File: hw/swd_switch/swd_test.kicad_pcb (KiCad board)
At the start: 2 copper layers, 30 x 17 mm, 11 parts, among them J1 SWD_IN, J2 Conn_01x04, J3 SWD_PWR, J4 SWD_OUT, U1 SN74LVC2G66, U2 SN74LVC2G66, U3 SN74LVC2G66

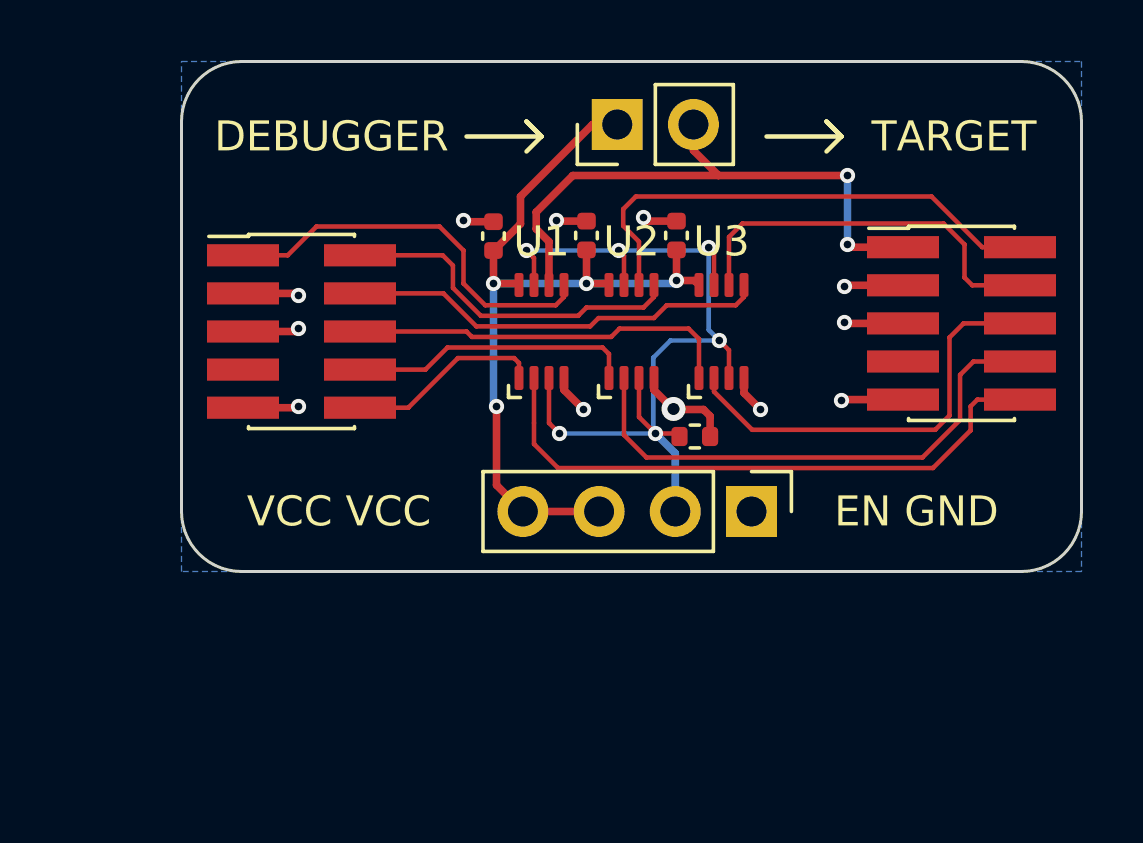
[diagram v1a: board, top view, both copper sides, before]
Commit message: Updated debugotron v2.0 and ordered
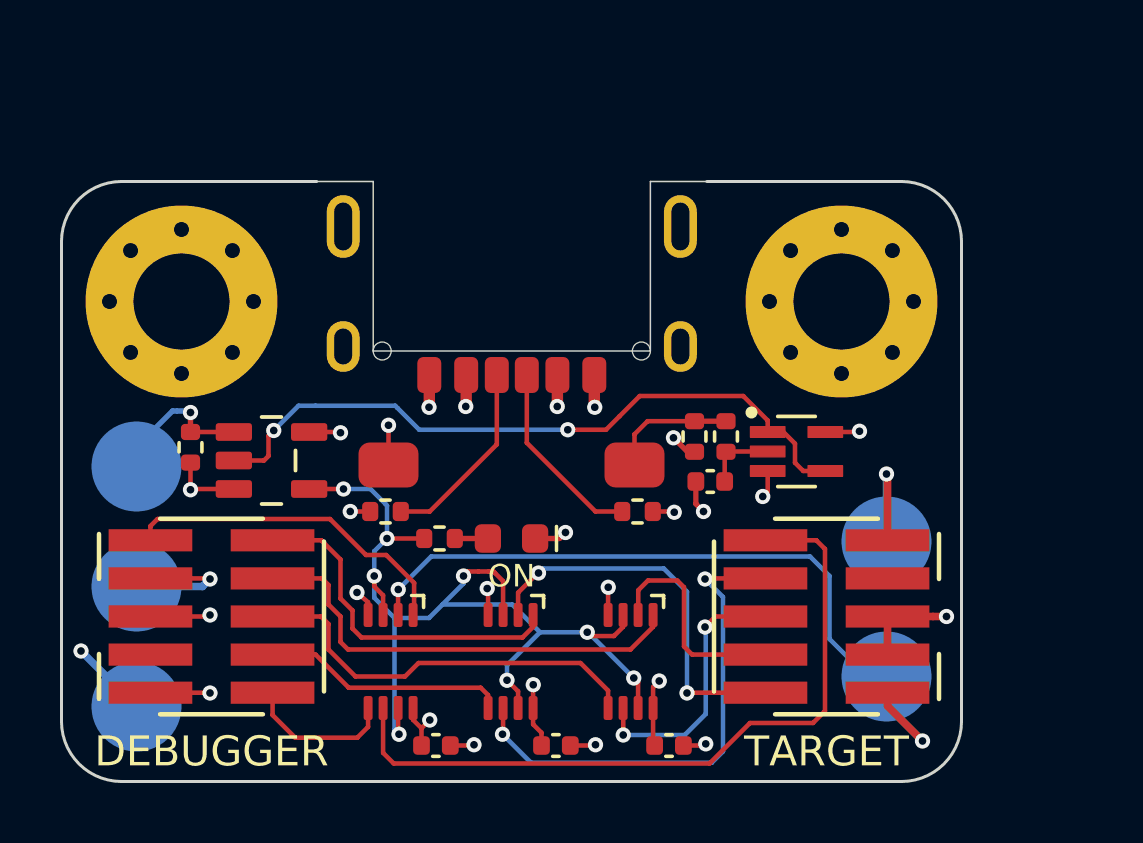
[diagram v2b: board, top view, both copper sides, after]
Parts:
- removed J1: SWD_IN, Connector_PinHeader_1.27mm:PinHeader_2x05_P1.27mm_Vertical_SMD
- removed J4: SWD_OUT, Connector_PinHeader_1.27mm:PinHeader_2x05_P1.27mm_Vertical_SMD
- added C4: 0.1uF, Capacitor_SMD:C_0402_1005Metric, F.Cu at (107.5, 73.8)
- added D1: LED, LED_SMD:LED_0603_1608Metric, F.Cu at (106.0, 66.9)
- added J5: SWD_OUT, snapeda:SAMTEC_FTSH-105-01-F-DV-P-TR_alt, F.Cu at (116.5, 69.5)
- added R1: 5.1k, Resistor_SMD:R_0402_1005Metric, F.Cu at (112.1, 63.5)
- added R3: 5.1k, Resistor_SMD:R_0402_1005Metric, F.Cu at (95.3, 63.9)
- added R4: 5.1k, Resistor_SMD:R_0402_1005Metric, F.Cu at (101.8, 66.0)
- added R5: 5.1k, Resistor_SMD:R_0402_1005Metric, F.Cu at (110.2, 66.0)
- added R6: 5.1k, Resistor_SMD:R_0402_1005Metric, F.Cu at (103.6, 66.9)
- added REF**: MountingHole_3.2mm_M3_Pad_Via, MountingHole:MountingHole_3.2mm_M3_Pad_Via, F.Cu at (117.0, 59.0)
- added REF**: MountingHole_3.2mm_M3_Pad_Via, MountingHole:MountingHole_3.2mm_M3_Pad_Via, F.Cu at (95.0, 59.0)
- added SW1: SW_Push, alvarop:PTS636_G, F.Cu at (106.0, 64.5)
- added TP1: TestPoint, TestPoint:TestPoint_Pad_D3.0mm, B.Cu at (93.5, 72.5)
- added TP2: TestPoint, TestPoint:TestPoint_Pad_D3.0mm, B.Cu at (93.5, 68.5)
- added TP3: TestPoint, TestPoint:TestPoint_Pad_D3.0mm, B.Cu at (93.5, 64.5)
- added TP4: TestPoint, TestPoint:TestPoint_Pad_D3.0mm, B.Cu at (118.5, 67.0)
- added TP5: TestPoint, TestPoint:TestPoint_Pad_D3.0mm, B.Cu at (118.5, 71.5)
- added U4: SN74LVC2G66, alvarop:SN74LVC2G66-VSSOP, F.Cu at (102.0, 71.0)
- added U5: SN74LVC2G66, alvarop:SN74LVC2G66-VSSOP, F.Cu at (106.0, 71.0)
- J2: value Conn_01x04 -> USB_C_Receptacle_USB2.0; footprint Connector_PinHeader_2.54mm:PinHeader_1x04_P2.54mm_Vertical -> alvarop:USB4515-GF-A
- J3: value SWD_PWR -> SWD_IN; footprint Connector_PinHeader_2.54mm:PinHeader_1x02_P2.54mm_Vertical -> snapeda:SAMTEC_FTSH-105-01-F-DV-P-TR_alt
- R2: value 10k -> 5.1k
- U1: value SN74LVC2G66 -> SN74LVC1G80DCKR; footprint alvarop:SN74LVC2G66-VSSOP -> snapeda:SOT65P210X110-5N
- U2: value SN74LVC2G66 -> SN74LVC1G32DBVR; footprint alvarop:SN74LVC2G66-VSSOP -> snapeda:SOT95P280X145-5N
- moved J3 21.3 mm to (96.0, 69.5), turned to -90 degrees
- moved C2 17.7 mm to (103.5, 73.8), turned to 0 degrees
- moved C3 17.0 mm to (111.2, 73.8), turned to 0 degrees
- moved U2 12.7 mm to (98.0, 64.3)
- moved U3 11.4 mm to (110.0, 71.0), turned to 180 degrees
- moved C1 10.9 mm to (112.6, 65.0), turned to 0 degrees
- moved J2 9.70 mm to (106.0, 60.5), turned to 180 degrees
- moved U1 9.39 mm to (115.5, 64.0)
- moved R2 1.04 mm to (113.2, 63.5), turned to -90 degrees
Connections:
- C1 pad 2: GND -> Net-(C1-Pad2)
- J3 pad 1: VCC -> /VREF
- J3 pad 2: /VREF_OUT -> /SWDIO_TMS
- R2 pad 1: /SWD_EN -> Net-(R1-Pad1)
- R2 pad 2: GND -> Net-(C1-Pad2)
- U1 pad 1: /RESET -> /SWD_EN_BTN
- U1 pad 2: /RESET_OUT -> Net-(C1-Pad2)
- U1 pad 3: /SWD_EN -> GND
- U1 pad 4: GND -> /SWD_EN_BTN
- U1 pad 5: /VREF -> VCC
- U2 pad 1: /TDI -> /SWD_EN_EXT
- U2 pad 2: /TDI_OUT -> /SWD_EN_BTN
- U2 pad 3: /SWD_EN -> GND
- U2 pad 4: GND -> /SWD_EN
- U2 pad 5: /SWDIO_TMS -> VCC
- U3 pad 1: /SWO_TDO -> /SWDCLK_TCK
- U3 pad 2: /SWO_TDO_OUT -> /SWDCLK_TCK_OUT
- U3 pad 5: /SWDCLK_TCK -> /SWO_TDO
- U3 pad 6: /SWDCLK_TCK_OUT -> /SWO_TDO_OUT
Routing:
- net /SWD_EN_BTN: track 0.00 -> 23.3 mm, vias 0 -> 2
- net VCC: track 28.8 -> 15.5 mm, vias 4 -> 10
- net GND: track 20.7 -> 30.2 mm, vias 12 -> 19
- net Net-(J2-PadB5): track 0.00 -> 6.44 mm
- net Net-(J2-PadA5): track 0.00 -> 6.39 mm
- net /SWDCLK_TCK_OUT: track 13.0 -> 7.38 mm
- net /VREF_OUT: track 19.7 -> 25.2 mm
- net /SWO_TDO_OUT: track 14.2 -> 9.01 mm, vias 0 -> 2
- net /RESET_OUT: track 20.1 -> 24.6 mm
- net /SWD_EN_EXT: track 0.00 -> 4.41 mm, vias 0 -> 1
- net Net-(R1-Pad1): track 0.00 -> 4.18 mm
- net /SWDIO_TMS_OUT: track 16.8 -> 13.0 mm, vias 0 -> 2
- net /SWD_EN: track 29.8 -> 33.4 mm, vias 6 -> 8
- net Net-(C1-Pad2): track 0.00 -> 2.42 mm
- net /VREF: track 13.3 -> 11.3 mm
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- added copper zone on In1.Cu, net GND
- added copper zone on In2.Cu, net VCC
- removed copper zone on B.Cu, net GND
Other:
- board size 30 x 17 mm -> 30 x 20 mm
- copper layers 2 -> 4
- rule pad_to_mask_clearance: 0.0508 -> 0
- board text added: "ENABLE GND VCC"
- board text added: "GND VREF"
- board text added: "ON"
- board text added: "SWD Switch 2.0"
- board text removed: "EN GND"
- board text removed: "SWD Switch 1.0"
- board text removed: "VCC VCC"

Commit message: Updated SWD switch to 2.1
Added schmitt trigger buffer to debounce circuit
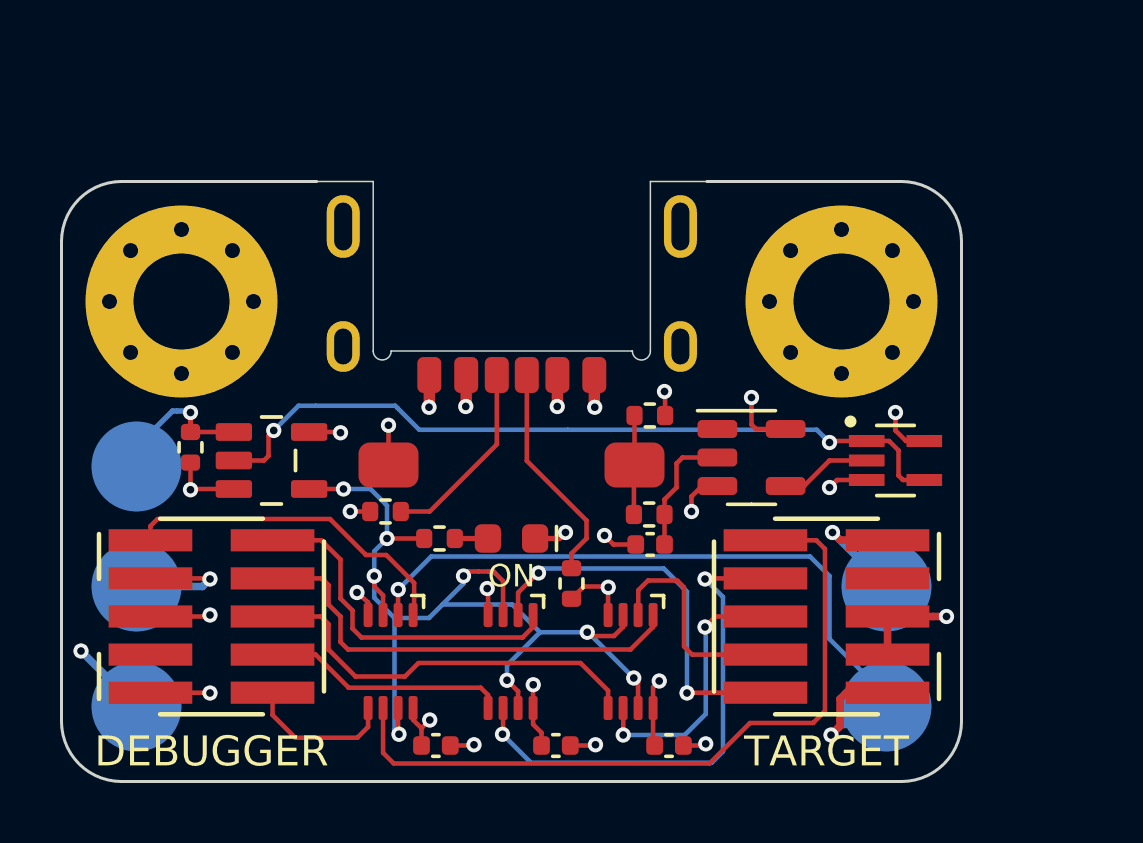
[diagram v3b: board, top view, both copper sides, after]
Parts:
- added U6: SN74AHC1G14, Package_TO_SOT_SMD:SOT-23-5, F.Cu at (114.0, 64.2)
- moved R2 3.65 mm to (110.6, 66.1), turned to 0 degrees
- moved U1 3.31 mm to (118.8, 64.3)
- moved R5 3.26 mm to (108.0, 68.4), turned to -90 degrees
- moved C1 2.90 mm to (110.6, 67.1), turned to 180 degrees
- moved R1 1.65 mm to (110.6, 62.8), turned to 180 degrees
- moved TP4 1.50 mm to (118.5, 68.5)
- moved TP5 1.00 mm to (118.5, 72.5)
- turned SW1 to 0 degrees
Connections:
- C1 pad 1: VCC -> Net-(R2-Pad2)
- C1 pad 2: Net-(C1-Pad2) -> GND
- R1 pad 1: Net-(R1-Pad1) -> VCC
- R1 pad 2: GND -> Net-(R2-Pad1)
- R2 pad 1: Net-(R1-Pad1) -> Net-(R2-Pad1)
- R2 pad 2: Net-(C1-Pad2) -> Net-(R2-Pad2)
- SW1 pad 1: Net-(R1-Pad1) -> GND
- SW1 pad 2: VCC -> Net-(R2-Pad1)
- U1 pad 2: Net-(C1-Pad2) -> Net-(U1-Pad2)
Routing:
- net Net-(R2-Pad2): track 0.00 -> 4.31 mm
- net Net-(R1-Pad1): track 4.18 -> 0.00 mm
- net GND: track 30.2 -> 34.4 mm, vias 19 -> 20
- net Net-(R2-Pad1): track 0.00 -> 3.31 mm
- net Net-(U1-Pad2): track 0.00 -> 3.05 mm
- net /SWD_EN_BTN: track 23.3 -> 25.7 mm
- net Net-(C1-Pad2): track 2.42 -> 0.00 mm
- net /VREF_OUT: track 25.2 -> 26.7 mm
- net Net-(J2-PadA5): track 6.39 -> 7.47 mm
- net VCC: track 15.5 -> 16.5 mm
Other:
- board text added: "SWD Switch 2.1"
- board text removed: "SWD Switch 2.0"
